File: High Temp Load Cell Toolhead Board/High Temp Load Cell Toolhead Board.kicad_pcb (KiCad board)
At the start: 6 copper layers, 60 x 60 mm, 123 parts, among them J1 Conn_01x03, J11 Conn_01x03, J12 Conn_01x03, J13 PinHeader_2x4_P2.54mm, J2 Conn_02x08, J6 Conn_01x04, J7 Conn_01x02, J8 Conn_01x04, J9 Conn_01x02, P1 USB_C_Plug_USB2.0, Q1 CSD17581Q3A, Q2 CSD17581Q3A, SW1 SW_SPST, U1 SN74LVC2G17DSFR, U2 STM32F103CBU6TR, U3 SN74LVC2G17DSFR, U5 ADS1220, Y1 Crystal

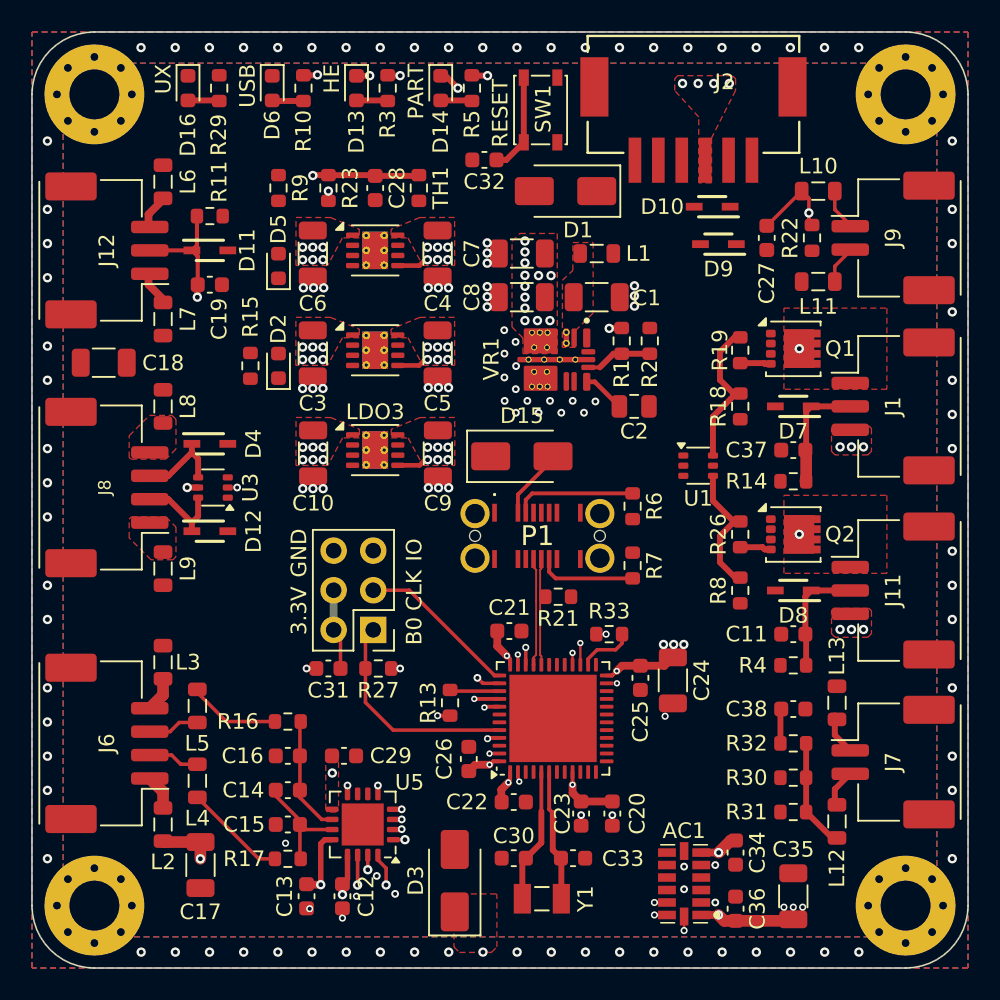
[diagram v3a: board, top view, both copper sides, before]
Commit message: Feedback Updates Completed
* Disconnected unused GPIO pins from ground, use software pulldown instead.
* Re-rout for OSHPark's 6 layer stackup
* Shrink reference text to 0.8mmx0.8mm and 5 mil thickness
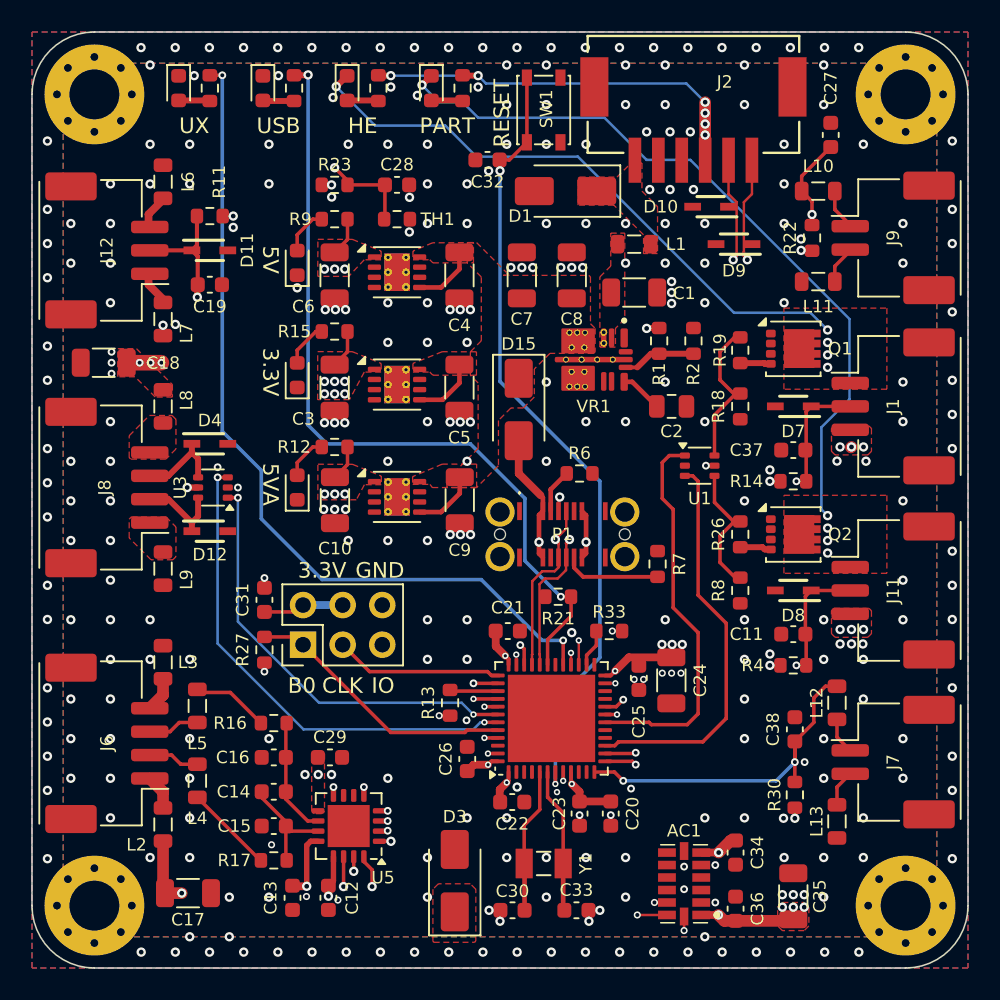
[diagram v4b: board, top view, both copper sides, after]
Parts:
- removed R31: R2.2kΩ, Resistor_SMD:R_0603_1608Metric
- removed R32: R4.7kΩ, Resistor_SMD:R_0603_1608Metric
- added D17: RED LED, LED_SMD:LED_0603_1608Metric, F.Cu at (17.0, 29.2)
- added R12: R2kΩ, Resistor_SMD:R_0603_1608Metric, F.Cu at (19.4, 26.6)
- moved C27 7.77 mm to (51.2, 6.60), turned to 90 degrees
- moved L12 7.60 mm to (51.6, 43.0), turned to -90 degrees
- moved L13 7.60 mm to (51.6, 50.6), turned to -90 degrees
- moved R27 7.40 mm to (14.9, 39.6), turned to -90 degrees
- moved C31 6.01 mm to (14.9, 36.4), turned to 90 degrees
- moved R15 5.83 mm to (19.4, 19.2), turned to 180 degrees
- moved J13 4.60 mm to (17.4, 39.3), turned to 90 degrees
- moved R9 4.12 mm to (19.4, 12.0), turned to 0 degrees
- moved R6 4.00 mm to (35.1, 28.3), turned to 0 degrees
- moved C8 3.49 mm to (34.6, 15.6), turned to 90 degrees
- moved C33 3.35 mm to (34.9, 56.3)
- moved C30 3.34 mm to (30.8, 56.3)
- moved C10 3.31 mm to (19.4, 30.0)
- moved C9 3.31 mm to (27.4, 30.0)
- moved LDO3 3.31 mm to (23.4, 29.8)
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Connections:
- net Net-(U5-AIN0/REFP1) renamed /AIN0
- net Net-(U5-AIN1) renamed /AIN1
- C38 pad 1: PT1000 -> HOTEND_THERMISTOR
- J7 pad 1: /PT1000- -> /HOTEND_TH_VREF
- J7 pad 2: /PT1000+ -> /HOTEND_TH_GND
- L12 pad 1: Net-(L12-Pad1) -> HOTEND_THERMISTOR
- L12 pad 2: /PT1000+ -> /HOTEND_TH_VREF
- L13 pad 1: /PT1000- -> /HOTEND_TH_GND
- R30 pad 1: Net-(L12-Pad1) -> HOTEND_THERMISTOR
- U2 pad 10: GND -> unconnected-(U2-PA0-Pad10)
- U2 pad 11: GND -> unconnected-(U2-PA1-Pad11)
- U2 pad 12: PT1000 -> HOTEND_THERMISTOR
- U2 pad 14: FAN1_PWM -> FAN0_TACH
- U2 pad 15: GND -> FAN1_PWM
- U2 pad 16: GND -> unconnected-(U2-PA6-Pad16)
- U2 pad 17: FAN0_TACH -> unconnected-(U2-PA7-Pad17)
- U2 pad 2: GND -> unconnected-(U2-PC13-Pad2)
- U2 pad 21: GND -> unconnected-(U2-PB10-Pad21)
- U2 pad 22: GND -> unconnected-(U2-PB11-Pad22)
- U2 pad 25: GND -> unconnected-(U2-PB12-Pad25)
- U2 pad 3: GND -> unconnected-(U2-PC14-Pad3)
- U2 pad 30: GND -> unconnected-(U2-PA9-Pad30)
- U2 pad 4: GND -> unconnected-(U2-PC15-Pad4)
- U2 pad 46: GND -> unconnected-(U2-PB9-Pad46)
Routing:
- net +5V: track 0.70 -> 63.7 mm, vias 7 -> 8
- net AMBIENT_THERMISTOR: track 6.85 -> 62.0 mm, vias 1 -> 2
- net INDICATOR_LED: track 0.00 -> 54.4 mm, vias 0 -> 2
- net USB_PULL_UP: track 0.88 -> 52.1 mm, vias 1 -> 2
- net +5VA: track 7.89 -> 58.8 mm, vias 9 -> 6
- net NRST: track 6.37 -> 51.0 mm, vias 0 -> 2
- net HEATBREAK_THERMISTOR: track 6.30 -> 46.2 mm, vias 1 -> 2
- net USB_D+: track 6.84 -> 44.8 mm, vias 0 -> 3
- net USB_D-: track 6.93 -> 40.9 mm, vias 0 -> 2
- net LED_MCU_CLK: track 0.00 -> 31.7 mm, vias 0 -> 2
- net LED_MCU_SDO: track 0.00 -> 27.7 mm, vias 0 -> 2
- net FAN0_TACH: track 7.46 -> 34.8 mm, vias 0 -> 2
- net FAN1_PWM: track 0.00 -> 25.4 mm
- net FAN0_PWM: track 0.00 -> 25.0 mm
- net HOTEND_THERMISTOR: track 0.00 -> 22.2 mm, vias 0 -> 2
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- added copper zone on In3.Cu, net +3V3
- added copper zone on F.Cu, net /+24V_INPUT
- removed copper zone on In2.Cu, net +5V5
- removed copper zone on In3.Cu, net GND
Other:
- board text added: "5VA"
- board text added: "HOT END"
- board text removed: "HE Fan"
- board text removed: "MCU STATUS"
- board text removed: "PT100"
